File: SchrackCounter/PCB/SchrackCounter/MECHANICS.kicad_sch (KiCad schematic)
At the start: 22 parts, among them J3 MEM2067-02-180-00-A_REVB, SW1 SW_Push, SW2 SW_Push, SW3 SW_Push, SW4 SW_Push, SW5 SW_Push

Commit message: PCB update
pcb redesign
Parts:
- renumbered J3 to J2, R10 to R12, R11 to R13, R12 to R14, R13 to R15, R14 to R16, SW1 to SW2, SW2 to SW3, SW3 to SW4, SW4 to SW5, SW5 to SW6
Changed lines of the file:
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@@
 		(on_board yes)
 		(dnp no)
-		(property "Reference" "#PWR029"
+		(property "Reference" "#PWR032"
 			(at 114.3 39.37 0)
 			(effects
@@
 			(project "SchrackCounter"
 				(path "/d96f2ffc-3f4c-4f71-b693-29f6b8c3245d/0ccd8f36-c6f2-454f-91e2-c1976b699e0e"
-					(reference "#PWR029")
+					(reference "#PWR032")
 					(unit 1)
 				)
@@
 		(on_board yes)
 		(dnp no)
-		(property "Reference" "#PWR024"
+		(property "Reference" "#PWR027"
 			(at 64.77 118.11 0)
 			(effects
@@
 			(project "SchrackCounter"
 				(path "/d96f2ffc-3f4c-4f71-b693-29f6b8c3245d/0ccd8f36-c6f2-454f-91e2-c1976b699e0e"
-					(reference "#PWR024")
+					(reference "#PWR027")
 					(unit 1)
 				)
@@
 		(on_board yes)
 		(dnp no)
-		(property "Reference" "#PWR036"
+		(property "Reference" "#PWR039"
 			(at 223.52 129.54 0)
 			(effects
@@
 			(project "SchrackCounter"
 				(path "/d96f2ffc-3f4c-4f71-b693-29f6b8c3245d/0ccd8f36-c6f2-454f-91e2-c1976b699e0e"
-					(reference "#PWR036")
+					(reference "#PWR039")
 					(unit 1)
 				)
@@
 		(on_board yes)
 		(dnp no)
-		(property "Reference" "#PWR034"
+		(property "Reference" "#PWR037"
 			(at 215.9 99.06 0)
 			(effects
@@
 			(project "SchrackCounter"
 				(path "/d96f2ffc-3f4c-4f71-b693-29f6b8c3245d/0ccd8f36-c6f2-454f-91e2-c1976b699e0e"
-					(reference "#PWR034")
+					(reference "#PWR037")
 					(unit 1)
 				)
@@
 		(on_board yes)
 		(dnp no)
-		(property "Reference" "R11"
+		(property "Reference" "R13"
 			(at 95.885 99.06 0)
 			(effects
@@
 			(project "SchrackCounter"
 				(path "/d96f2ffc-3f4c-4f71-b693-29f6b8c3245d/0ccd8f36-c6f2-454f-91e2-c1976b699e0e"
-					(reference "R11")
+					(reference "R13")
 					(unit 1)
 				)
@@
 		(on_board yes)
 		(dnp no)
-		(property "Reference" "R13"
+		(property "Reference" "R15"
 			(at 127.635 99.06 0)
 			(effects
@@
 			(project "SchrackCounter"
 				(path "/d96f2ffc-3f4c-4f71-b693-29f6b8c3245d/0ccd8f36-c6f2-454f-91e2-c1976b699e0e"
-					(reference "R13")
+					(reference "R15")
 					(unit 1)
 				)
@@
 		(on_board yes)
 		(dnp no)
-		(property "Reference" "#PWR033"
+		(property "Reference" "#PWR036"
 			(at 137.16 63.5 0)
 			(effects
@@
 			(project "SchrackCounter"
 				(path "/d96f2ffc-3f4c-4f71-b693-29f6b8c3245d/0ccd8f36-c6f2-454f-91e2-c1976b699e0e"
-					(reference "#PWR033")
+					(reference "#PWR036")
 					(unit 1)
 				)
@@
 		(on_board yes)
 		(dnp no)
-		(property "Reference" "SW3"
+		(property "Reference" "SW4"
 			(at 118.11 99.695 0)
 			(effects
@@
 			(project "SchrackCounter"
 				(path "/d96f2ffc-3f4c-4f71-b693-29f6b8c3245d/0ccd8f36-c6f2-454f-91e2-c1976b699e0e"
-					(reference "SW3")
+					(reference "SW4")
 					(unit 1)
 				)
@@
 		(on_board yes)
 		(dnp no)
-		(property "Reference" "#PWR032"
+		(property "Reference" "#PWR035"
 			(at 127 63.5 0)
 			(effects
@@
 			(project "SchrackCounter"
 				(path "/d96f2ffc-3f4c-4f71-b693-29f6b8c3245d/0ccd8f36-c6f2-454f-91e2-c1976b699e0e"
-					(reference "#PWR032")
+					(reference "#PWR035")
 					(unit 1)
 				)
@@
 		(on_board yes)
 		(dnp no)
-		(property "Reference" "#PWR022"
+		(property "Reference" "#PWR025"
 			(at 50.8 110.49 0)
 			(effects
@@
 			(project "SchrackCounter"
 				(path "/d96f2ffc-3f4c-4f71-b693-29f6b8c3245d/0ccd8f36-c6f2-454f-91e2-c1976b699e0e"
-					(reference "#PWR022")
+					(reference "#PWR025")
 					(unit 1)
 				)
@@
 		(on_board yes)
 		(dnp no)
-		(property "Reference" "#PWR026"
+		(property "Reference" "#PWR029"
 			(at 92.71 100.33 0)
 			(effects
@@
 			(project "SchrackCounter"
 				(path "/d96f2ffc-3f4c-4f71-b693-29f6b8c3245d/0ccd8f36-c6f2-454f-91e2-c1976b699e0e"
-					(reference "#PWR026")
+					(reference "#PWR029")
 					(unit 1)
 				)
@@
 		(on_board yes)
 		(dnp no)
-		(property "Reference" "#PWR027"
+		(property "Reference" "#PWR030"
 			(at 92.71 118.11 0)
 			(effects
@@
 			(project "SchrackCounter"
 				(path "/d96f2ffc-3f4c-4f71-b693-29f6b8c3245d/0ccd8f36-c6f2-454f-91e2-c1976b699e0e"
-					(reference "#PWR027")
+					(reference "#PWR030")
 					(unit 1)
 				)
@@
 		(on_board yes)
 		(dnp no)
-		(property "Reference" "#PWR025"
+		(property "Reference" "#PWR028"
 			(at 78.74 110.49 0)
 			(effects
@@
 			(project "SchrackCounter"
 				(path "/d96f2ffc-3f4c-4f71-b693-29f6b8c3245d/0ccd8f36-c6f2-454f-91e2-c1976b699e0e"
-					(reference "#PWR025")
+					(reference "#PWR028")
 					(unit 1)
 				)
@@
 		(on_board yes)
 		(dnp no)
-		(property "Reference" "#PWR031"
+		(property "Reference" "#PWR034"
 			(at 124.46 118.11 0)
 			(effects
@@
 			(project "SchrackCounter"
 				(path "/d96f2ffc-3f4c-4f71-b693-29f6b8c3245d/0ccd8f36-c6f2-454f-91e2-c1976b699e0e"
-					(reference "#PWR031")
+					(reference "#PWR034")
 					(unit 1)
 				)
@@
 		(on_board yes)
 		(dnp no)
-		(property "Reference" "SW2"
+		(property "Reference" "SW3"
 			(at 86.36 99.695 0)
 			(effects
@@
 			(project "SchrackCounter"
 				(path "/d96f2ffc-3f4c-4f71-b693-29f6b8c3245d/0ccd8f36-c6f2-454f-91e2-c1976b699e0e"
-					(reference "SW2")
+					(reference "SW3")
 					(unit 1)
 				)
@@
 		(on_board yes)
 		(dnp no)
-		(property "Reference" "R12"
+		(property "Reference" "R14"
 			(at 107.315 38.735 0)
 			(effects
@@
 			(project "SchrackCounter"
 				(path "/d96f2ffc-3f4c-4f71-b693-29f6b8c3245d/0ccd8f36-c6f2-454f-91e2-c1976b699e0e"
-					(reference "R12")
+					(reference "R14")
 					(unit 1)
 				)
@@
 		(on_board yes)
 		(dnp no)
-		(property "Reference" "#PWR037"
+		(property "Reference" "#PWR040"
 			(at 226.06 80.01 0)
 			(effects
@@
 			(project "SchrackCounter"
 				(path "/d96f2ffc-3f4c-4f71-b693-29f6b8c3245d/0ccd8f36-c6f2-454f-91e2-c1976b699e0e"
-					(reference "#PWR037")
+					(reference "#PWR040")
 					(unit 1)
 				)
@@
 		(on_board yes)
 		(dnp no)
-		(property "Reference" "J3"
+		(property "Reference" "J2"
 			(at 229.87 91.44 0)
 			(effects
@@
 			(project "SchrackCounter"
 				(path "/d96f2ffc-3f4c-4f71-b693-29f6b8c3245d/0ccd8f36-c6f2-454f-91e2-c1976b699e0e"
-					(reference "J3")
+					(reference "J2")
 					(unit 1)
 				)
@@
 		(on_board yes)
 		(dnp no)
-		(property "Reference" "#PWR035"
+		(property "Reference" "#PWR038"
 			(at 218.44 62.23 0)
 			(effects
@@
 			(project "SchrackCounter"
 				(path "/d96f2ffc-3f4c-4f71-b693-29f6b8c3245d/0ccd8f36-c6f2-454f-91e2-c1976b699e0e"
-					(reference "#PWR035")
+					(reference "#PWR038")
 					(unit 1)
 				)
@@
 		(on_board yes)
 		(dnp no)
-		(property "Reference" "R10"
+		(property "Reference" "R12"
 			(at 67.945 99.06 0)
 			(effects
@@
 			(project "SchrackCounter"
 				(path "/d96f2ffc-3f4c-4f71-b693-29f6b8c3245d/0ccd8f36-c6f2-454f-91e2-c1976b699e0e"
-					(reference "R10")
+					(reference "R12")
 					(unit 1)
 				)
@@
 		(on_board yes)
 		(dnp no)
-		(property "Reference" "#PWR030"
+		(property "Reference" "#PWR033"
 			(at 124.46 100.33 0)
 			(effects
@@
 			(project "SchrackCounter"
 				(path "/d96f2ffc-3f4c-4f71-b693-29f6b8c3245d/0ccd8f36-c6f2-454f-91e2-c1976b699e0e"
-					(reference "#PWR030")
+					(reference "#PWR033")
 					(unit 1)
 				)
@@
 		(on_board yes)
 		(dnp no)
-		(property "Reference" "SW5"
+		(property "Reference" "SW6"
 			(at 143.51 43.815 0)
 			(effects
@@
 			(project "SchrackCounter"
 				(path "/d96f2ffc-3f4c-4f71-b693-29f6b8c3245d/0ccd8f36-c6f2-454f-91e2-c1976b699e0e"
-					(reference "SW5")
+					(reference "SW6")
 					(unit 1)
 				)
@@
 		(on_board yes)
 		(dnp no)
-		(property "Reference" "#PWR028"
+		(property "Reference" "#PWR031"
 			(at 110.49 110.49 0)
 			(effects
@@
 			(project "SchrackCounter"
 				(path "/d96f2ffc-3f4c-4f71-b693-29f6b8c3245d/0ccd8f36-c6f2-454f-91e2-c1976b699e0e"
-					(reference "#PWR028")
+					(reference "#PWR031")
 					(unit 1)
 				)
@@
 		(on_board yes)
 		(dnp no)
-		(property "Reference" "R14"
+		(property "Reference" "R16"
 			(at 212.725 102.87 0)
 			(effects
@@
 			(project "SchrackCounter"
 				(path "/d96f2ffc-3f4c-4f71-b693-29f6b8c3245d/0ccd8f36-c6f2-454f-91e2-c1976b699e0e"
-					(reference "R14")
+					(reference "R16")
 					(unit 1)
 				)
@@
 		(on_board yes)
 		(dnp no)
-		(property "Reference" "SW1"
+		(property "Reference" "SW2"
 			(at 58.42 99.695 0)
 			(effects
@@
 			(project "SchrackCounter"
 				(path "/d96f2ffc-3f4c-4f71-b693-29f6b8c3245d/0ccd8f36-c6f2-454f-91e2-c1976b699e0e"
-					(reference "SW1")
+					(reference "SW2")
 					(unit 1)
 				)
@@
 		(on_board yes)
 		(dnp no)
-		(property "Reference" "#PWR023"
+		(property "Reference" "#PWR026"
 			(at 64.77 100.33 0)
 			(effects
@@
 			(project "SchrackCounter"
 				(path "/d96f2ffc-3f4c-4f71-b693-29f6b8c3245d/0ccd8f36-c6f2-454f-91e2-c1976b699e0e"
-					(reference "#PWR023")
+					(reference "#PWR026")
 					(unit 1)
 				)
@@
 		(on_board yes)
 		(dnp no)
-		(property "Reference" "SW4"
+		(property "Reference" "SW5"
 			(at 120.65 43.815 0)
 			(effects
@@
 			(project "SchrackCounter"
 				(path "/d96f2ffc-3f4c-4f71-b693-29f6b8c3245d/0ccd8f36-c6f2-454f-91e2-c1976b699e0e"
-					(reference "SW4")
-					(unit 1)
-				)
+					(reference "SW5")
+					(unit 1)
+				)

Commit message: PCB finalizing
Final routing and layout
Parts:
- C12: value 100nF.en -> 100nF
- C14: value 100nF.boot -> 100nF
- R14: value 10k.mcu -> 10k
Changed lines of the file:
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@@
 		(dnp no)
 		(property "Reference" "R14"
-			(at 107.315 38.735 0)
-			(effects
-				(font
-					(face "Bahnschrift")
-					(size 1.27 1.27)
-				)
-			)
-		)
-		(property "Value" "10k.mcu"
-			(at 109.22 41.275 0)
+			(at 111.125 39.37 0)
+			(effects
+				(font
+					(face "Bahnschrift")
+					(size 1.27 1.27)
+				)
+			)
+		)
+		(property "Value" "10k"
+			(at 111.125 41.91 0)
 			(effects
 				(font
@@
 			)
 		)
-		(property "Value" "100nF.en"
+		(property "Value" "100nF"
 			(at 125.095 58.42 90)
 			(effects
@@
 			)
 		)
-		(property "Value" "100nF.boot"
-			(at 139.7 58.42 90)
-			(effects
-				(font
+		(property "Value" "100nF"
+			(at 143.51 58.42 90)
+			(effects
+				(font

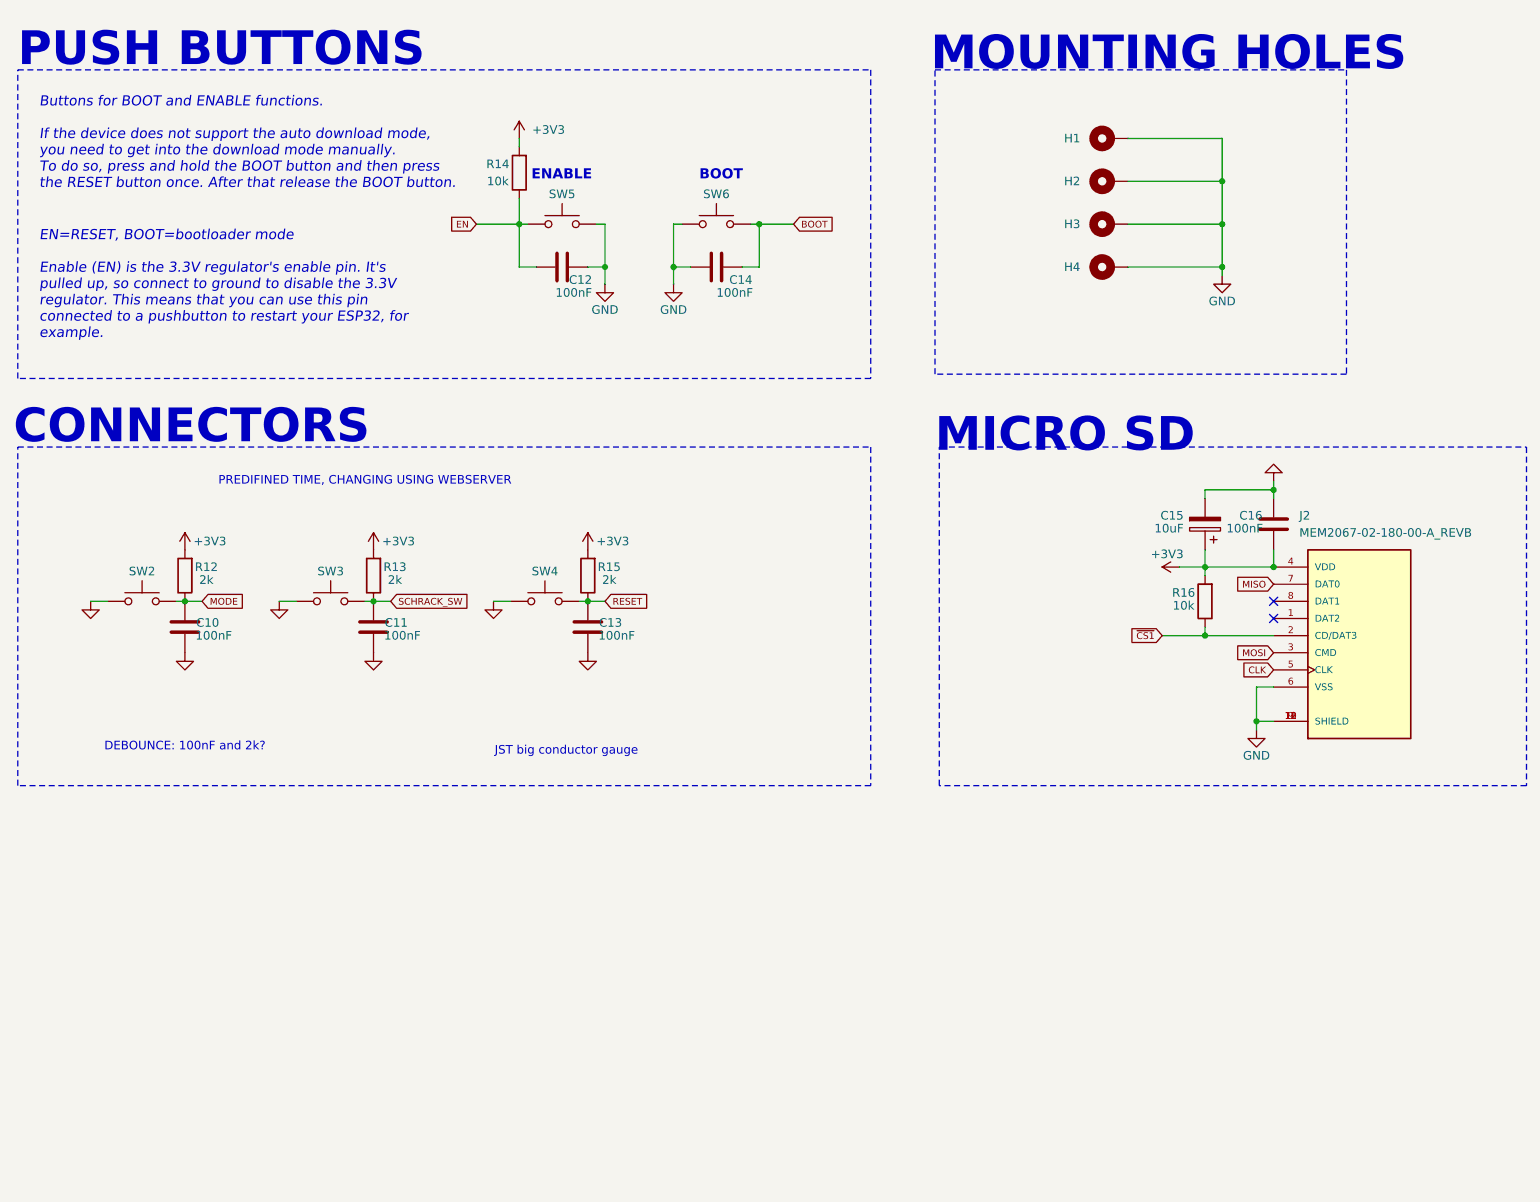
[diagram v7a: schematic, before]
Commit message: SchrackMulticlock and Counter update
Schematic update for both
PCB update for Counter
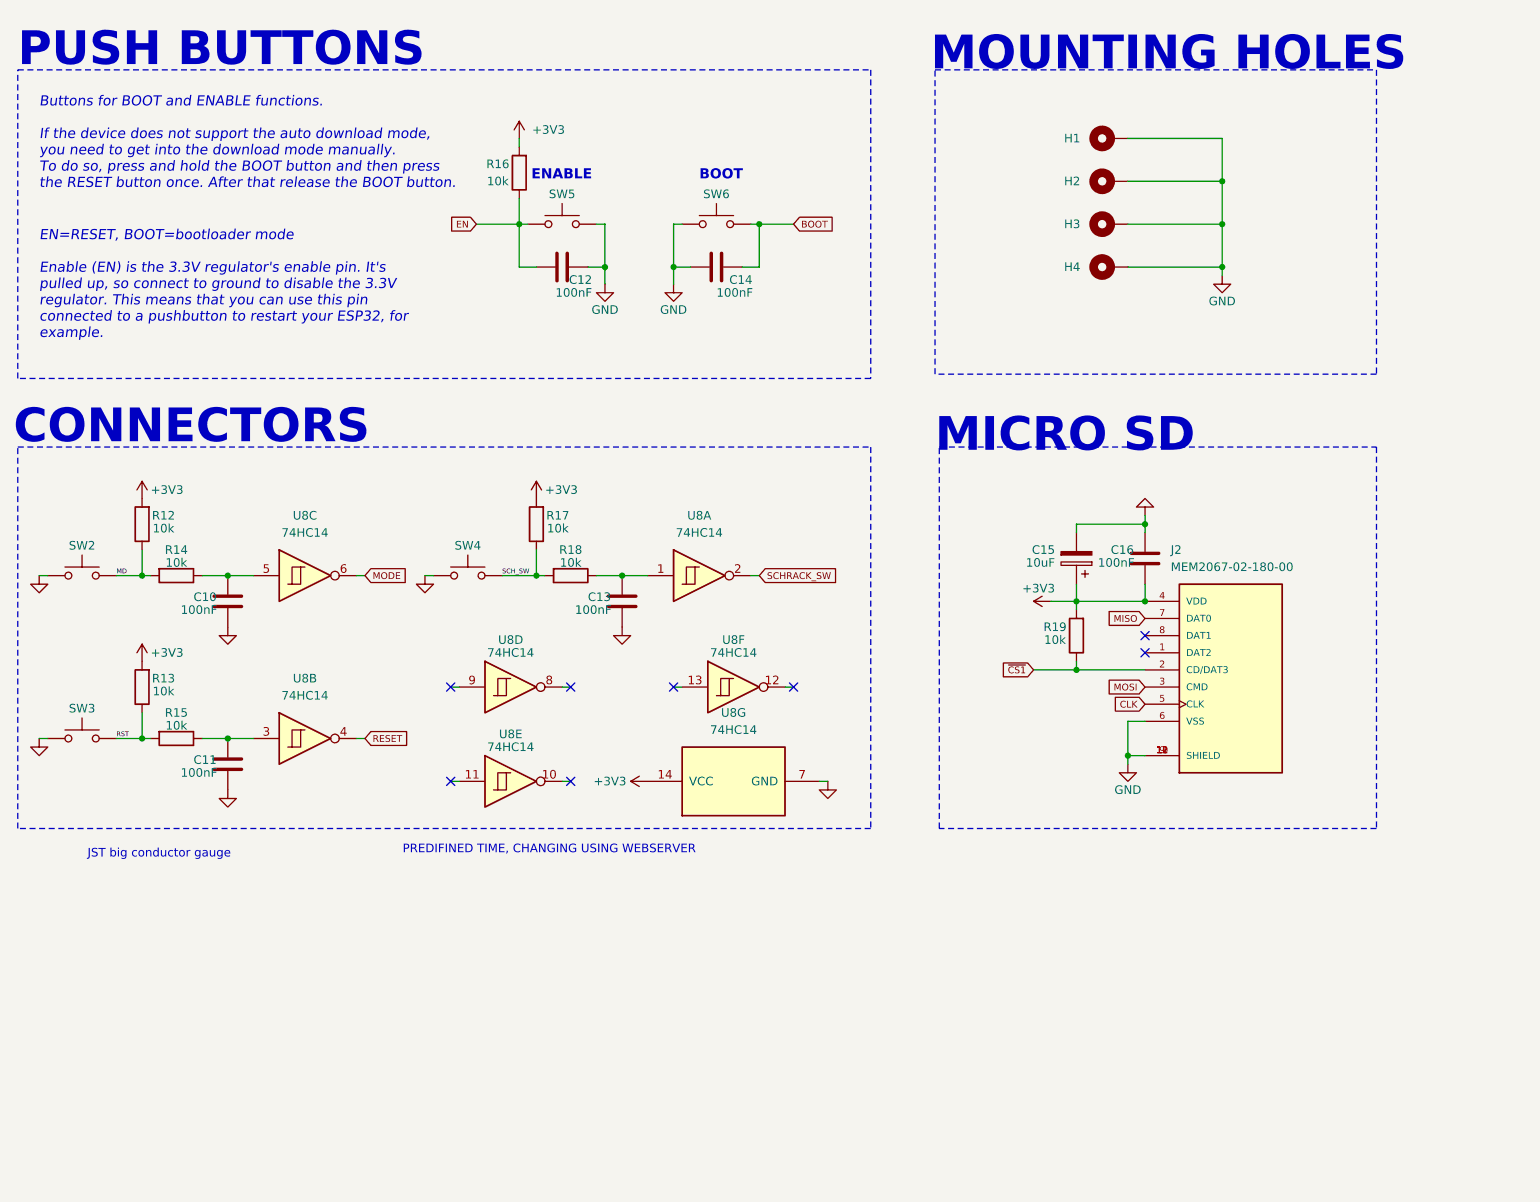
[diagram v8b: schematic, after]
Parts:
- added R14, R17, R18: 10k, Resistor_SMD:R_0805_2012Metric_Pad1.20x1.40mm_HandSolder, symbol Device:R
- added U8: 74HC14, Package_SO:SOIC-14_3.9x8.7mm_P1.27mm, symbol 74xx:74HC14
- J2: value MEM2067-02-180-00-A_REVB -> MEM2067-02-180-00
- R12, R13, R15: value 2k -> 10k
- renumbered R14 to R16, R16 to R19
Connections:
- net +3V3: now also R17.2, U8.14 (VCC); no longer R15.2
- net GND: now also U8.7 (GND)
- net MODE: now also U8.6; no longer C10.2, R12.1, SW2.2
- net RESET: now also U8.4; no longer C13.2, R15.1, SW4.2
- net SCHRACK_SW: now also U8.2; no longer C11.2, R13.1, SW3.2
- new net: C11.2, R15.1, U8.3
- new net: C10.2, R14.1, U8.5
- new net: C13.2, R18.1, U8.1
- new net MD: R12.1, R14.2, SW2.2
- new net RST: R13.1, R15.2, SW3.2
- new net SCH_SW: R17.1, R18.2, SW4.2
- no-connect marks 2 -> 8
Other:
- note removed: "DEBOUNCE: 100nF and 2k?"
- moved on the sheet: C10, C15, C16, J2, R19, SW2
